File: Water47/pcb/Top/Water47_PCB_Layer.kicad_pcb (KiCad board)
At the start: 2 copper layers, 260 x 76.5 mm, 51 parts, among them SW1 Esc, SW10 O, SW11 P, SW12 -, SW13 Del, SW14 Cmd, SW15 A, SW16 S, SW17 D, SW18 F, SW19 G, SW2 Q, SW20 H, SW21 J, SW22 K, SW23 L, SW24 ;, SW25 Bs, SW26 Shift(L), SW27 Z, SW28 X, SW29 C, SW3 W, SW30 V, SW31 B, SW32 N, SW33 M, SW34 ,, SW35 ., SW36 Shift(R), SW37 Fn, SW38 Ctrl(L), SW39 Win(L), SW4 E, SW40 Alt(L), SW41 Shift(C), SW42 Fn(C), SW43 Enter, SW44 ←, SW45 ↓, SW46 ↑, SW47 →, SW5 R, SW6 T, SW7 Y, SW8 U, SW9 I

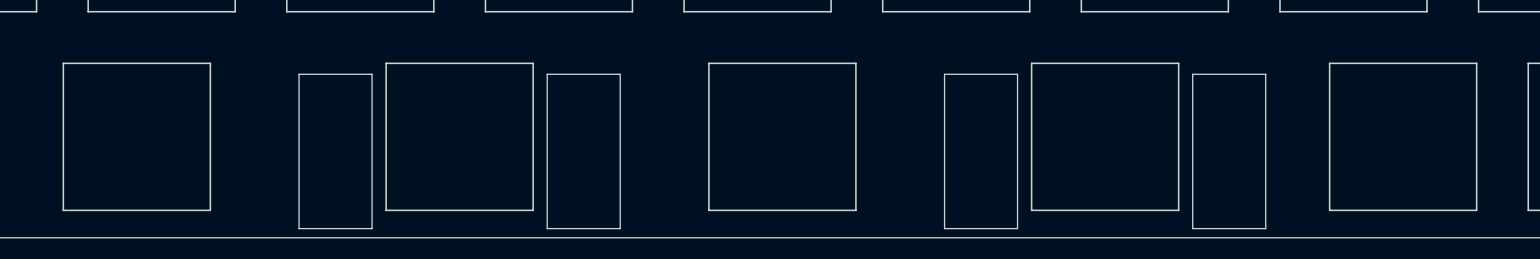
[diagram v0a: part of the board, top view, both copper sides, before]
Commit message: feat: change key layout
2u -> 1.75u to not put stabilizer
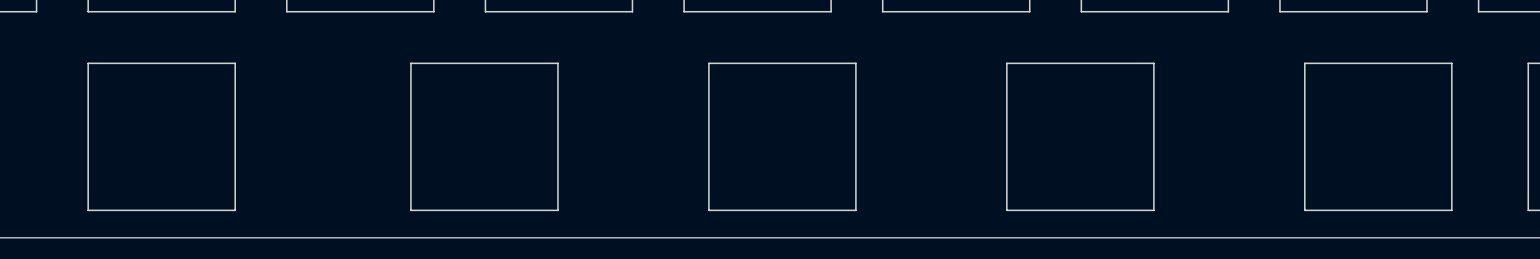
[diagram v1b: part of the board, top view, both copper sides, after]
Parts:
- SW40: footprint kbd_SW_Hole:SW_Hole_1.25u -> kbd_SW_Hole:SW_Hole_1.5u
- SW41, SW43: footprint kbd_SW_Hole:SW_Hole_2u -> kbd_SW_Hole:SW_Hole_1.75u
- SW44: footprint kbd_SW_Hole:SW_Hole_1u -> kbd_SW_Hole:SW_Hole_1.25u
- moved SW40 2.38 mm to (150.0, 150.0)
- moved SW44 2.38 mm to (266.7, 150.0)
- moved SW41 2.38 mm to (181.0, 150.0)
- moved SW43 2.38 mm to (238.1, 150.0)
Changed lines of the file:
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@@
   )
   (net 0 "")
-  (footprint "kbd_SW_Hole:SW_Hole_2u" (layer "F.Cu")
-    (at 178.59375 150.01875)
-    (property "Sheetfile" "Water47_PCB_Layer.kicad_sch")
-    (property "Sheetname" "")
-    (attr through_hole)
-    (fp_text reference "SW41" (at 7 8.1) (layer "Edge.Cuts") hide
+  (footprint "kbd_SW_Hole:SW_Hole_1.75u" (layer "F.Cu")
+    (at 180.975 150.01875)
+    (property "Sheetfile" "Water47_PCB_Layer.kicad_sch")
+    (property "Sheetname" "")
+    (attr through_hole)
+    (fp_text reference "SW41" (at 7 8.1) (layer "F.SilkS") hide
       (effects (font (size 1 1) (thickness 0.15)))
     )
@@
       (effects (font (size 1 1) (thickness 0.15)))
     )
-    (fp_line (start -8.4 -6) (end -8.4 8.8) (layer "Edge.Cuts") (width 0.12))
-    (fp_line (start -15.4 8.8) (end -15.4 -6) (layer "Edge.Cuts") (width 0.12))
-    (fp_line (start -8.4 8.8) (end -15.4 8.8) (layer "Edge.Cuts") (width 0.12))
-    (fp_line (start 15.4 -6) (end 8.4 -6) (layer "Edge.Cuts") (width 0.12))
-    (fp_line (start 7.05 7.05) (end -7.05 7.05) (layer "Edge.Cuts") (width 0.15))
-    (fp_line (start 7.05 -7.05) (end 7.05 7.05) (layer "Edge.Cuts") (width 0.15))
-    (fp_line (start 8.4 8.8) (end 15.4 8.8) (layer "Edge.Cuts") (width 0.12))
-    (fp_line (start -7.05 -7.05) (end 7.05 -7.05) (layer "Edge.Cuts") (width 0.15))
-    (fp_line (start 15.4 8.8) (end 15.4 -6) (layer "Edge.Cuts") (width 0.12))
-    (fp_line (start -15.4 -6) (end -8.4 -6) (layer "Edge.Cuts") (width 0.12))
-    (fp_line (start 8.4 -6) (end 8.4 8.8) (layer "Edge.Cuts") (width 0.12))
-    (fp_line (start -7.05 7.05) (end -7.05 -7.05) (layer "Edge.Cuts") (width 0.15))
-    (fp_line (start -19.05 9.525) (end 19.05 9.525) (layer "F.Fab") (width 0.15))
-    (fp_line (start 19.05 9.525) (end 19.05 -9.525) (layer "F.Fab") (width 0.15))
-    (fp_line (start -19.05 -9.525) (end -19.05 9.525) (layer "F.Fab") (width 0.15))
-    (fp_line (start 19.05 -9.525) (end -19.05 -9.525) (layer "F.Fab") (width 0.15))
+    (fp_line (start -7.05 7.05) (end -7.05 -7.05) (layer "Edge.Cuts") (width 0.15))
+    (fp_line (start 7.05 7.05) (end -7.05 7.05) (layer "Edge.Cuts") (width 0.15))
+    (fp_line (start -7.05 -7.05) (end 7.05 -7.05) (layer "Edge.Cuts") (width 0.15))
+    (fp_line (start 7.05 -7.05) (end 7.05 7.05) (layer "Edge.Cuts") (width 0.15))
+    (fp_line (start -16.66875 9.525) (end 16.66875 9.525) (layer "F.Fab") (width 0.15))
+    (fp_line (start -16.66875 -9.525) (end -16.66875 9.525) (layer "F.Fab") (width 0.15))
+    (fp_line (start 16.66875 -9.525) (end -16.66875 -9.525) (layer "F.Fab") (width 0.15))
+    (fp_line (start 16.66875 9.525) (end 16.66875 -9.525) (layer "F.Fab") (width 0.15))
   )
   (footprint "kbd_SW_Hole:SW_Hole_1u" (layer "F.Cu")
@@
     (fp_line (start 9.525 -9.525) (end -9.525 -9.525) (layer "F.Fab") (width 0.15))
   )
-  (footprint "kbd_SW_Hole:SW_Hole_1u" (layer "F.Cu")
-    (at 269.08125 150.01875)
+  (footprint "kbd_SW_Hole:SW_Hole_1.25u" (layer "F.Cu")
+    (at 266.7 150.01875)
     (property "Sheetfile" "Water47_PCB_Layer.kicad_sch")
     (property "Sheetname" "")
@@
       (effects (font (size 1 1) (thickness 0.15)))
     )
-    (fp_line (start 7.05 -7.05) (end 7.05 7.05) (layer "Edge.Cuts") (width 0.15))
-    (fp_line (start -7.05 7.05) (end -7.05 -7.05) (layer "Edge.Cuts") (width 0.15))
-    (fp_line (start 7.05 7.05) (end -7.05 7.05) (layer "Edge.Cuts") (width 0.15))
-    (fp_line (start -7.05 -7.05) (end 7.05 -7.05) (layer "Edge.Cuts") (width 0.15))
-    (fp_line (start -9.525 9.525) (end 9.525 9.525) (layer "F.Fab") (width 0.15))
-    (fp_line (start -9.525 -9.525) (end -9.525 9.525) (layer "F.Fab") (width 0.15))
-    (fp_line (start 9.525 -9.525) (end -9.525 -9.525) (layer "F.Fab") (width 0.15))
-    (fp_line (start 9.525 9.525) (end 9.525 -9.525) (layer "F.Fab") (width 0.15))
+    (fp_line (start -7.05 -7.05) (end 7.05 -7.05) (layer "Edge.Cuts") (width 0.15))
+    (fp_line (start 7.05 -7.05) (end 7.05 7.05) (layer "Edge.Cuts") (width 0.15))
+    (fp_line (start 7.05 7.05) (end -7.05 7.05) (layer "Edge.Cuts") (width 0.15))
+    (fp_line (start -7.05 7.05) (end -7.05 -7.05) (layer "Edge.Cuts") (width 0.15))
+    (fp_line (start -11.90625 -9.525) (end -11.90625 9.525) (layer "F.Fab") (width 0.15))
+    (fp_line (start 11.90625 -9.525) (end -11.90625 -9.525) (layer "F.Fab") (width 0.15))
+    (fp_line (start 11.90625 9.525) (end 11.90625 -9.525) (layer "F.Fab") (width 0.15))
+    (fp_line (start -11.90625 9.525) (end 11.90625 9.525) (layer "F.Fab") (width 0.15))
   )
   (footprint "kbd_SW_Hole:SW_Hole_1u" (layer "F.Cu")
@@
     (fp_line (start -16.66875 -9.525) (end -16.66875 9.525) (layer "F.Fab") (width 0.15))
   )
-  (footprint "kbd_SW_Hole:SW_Hole_1.25u" (layer "F.Cu")
-    (at 147.6375 150.01875)
+  (footprint "kbd_SW_Hole:SW_Hole_1.5u" (layer "F.Cu")
+    (at 150.01875 150.01875)
     (property "Sheetfile" "Water47_PCB_Layer.kicad_sch")
     (property "Sheetname" "")
@@
     (fp_line (start -7.05 7.05) (end -7.05 -7.05) (layer "Edge.Cuts") (width 0.15))
     (fp_line (start 7.05 7.05) (end -7.05 7.05) (layer "Edge.Cuts") (width 0.15))
-    (fp_line (start 11.90625 -9.525) (end -11.90625 -9.525) (layer "F.Fab") (width 0.15))
-    (fp_line (start -11.90625 9.525) (end 11.90625 9.525) (layer "F.Fab") (width 0.15))
-    (fp_line (start -11.90625 -9.525) (end -11.90625 9.525) (layer "F.Fab") (width 0.15))
-    (fp_line (start 11.90625 9.525) (end 11.90625 -9.525) (layer "F.Fab") (width 0.15))
+    (fp_line (start -14.2875 -9.525) (end -14.2875 9.525) (layer "F.Fab") (width 0.15))
+    (fp_line (start 14.2875 -9.525) (end -14.2875 -9.525) (layer "F.Fab") (width 0.15))
+    (fp_line (start 14.2875 9.525) (end 14.2875 -9.525) (layer "F.Fab") (width 0.15))
+    (fp_line (start -14.2875 9.525) (end 14.2875 9.525) (layer "F.Fab") (width 0.15))
   )
   (footprint "kbd_SW_Hole:SW_Hole_1u" (layer "F.Cu")
@@
     (fp_line (start 9.525 -9.525) (end -9.525 -9.525) (layer "F.Fab") (width 0.15))
   )
-  (footprint "kbd_SW_Hole:SW_Hole_2u" (layer "F.Cu")
-    (at 240.5 150.01875)
-    (property "Sheetfile" "Water47_PCB_Layer.kicad_sch")
-    (property "Sheetname" "")
-    (attr through_hole)
-    (fp_text reference "SW43" (at 7 8.1) (layer "Edge.Cuts") hide
+  (footprint "kbd_SW_Hole:SW_Hole_1.75u" (layer "F.Cu")
+    (at 238.125 150.01875)
+    (property "Sheetfile" "Water47_PCB_Layer.kicad_sch")
+    (property "Sheetname" "")
+    (attr through_hole)
+    (fp_text reference "SW43" (at 7 8.1) (layer "F.SilkS") hide
       (effects (font (size 1 1) (thickness 0.15)))
     )
@@
       (effects (font (size 1 1) (thickness 0.15)))
     )
-    (fp_line (start -7.05 7.05) (end -7.05 -7.05) (layer "Edge.Cuts") (width 0.15))
-    (fp_line (start -8.4 8.8) (end -15.4 8.8) (layer "Edge.Cuts") (width 0.12))
-    (fp_line (start 7.05 7.05) (end -7.05 7.05) (layer "Edge.Cuts") (width 0.15))
-    (fp_line (start 15.4 -6) (end 8.4 -6) (layer "Edge.Cuts") (width 0.12))
-    (fp_line (start -15.4 8.8) (end -15.4 -6) (layer "Edge.Cuts") (width 0.12))
-    (fp_line (start 8.4 8.8) (end 15.4 8.8) (layer "Edge.Cuts") (width 0.12))
-    (fp_line (start -15.4 -6) (end -8.4 -6) (layer "Edge.Cuts") (width 0.12))
-    (fp_line (start 7.05 -7.05) (end 7.05 7.05) (layer "Edge.Cuts") (width 0.15))
-    (fp_line (start 8.4 -6) (end 8.4 8.8) (layer "Edge.Cuts") (width 0.12))
-    (fp_line (start 15.4 8.8) (end 15.4 -6) (layer "Edge.Cuts") (width 0.12))
-    (fp_line (start -8.4 -6) (end -8.4 8.8) (layer "Edge.Cuts") (width 0.12))
-    (fp_line (start -7.05 -7.05) (end 7.05 -7.05) (layer "Edge.Cuts") (width 0.15))
-    (fp_line (start 19.05 9.525) (end 19.05 -9.525) (layer "F.Fab") (width 0.15))
-    (fp_line (start -19.05 -9.525) (end -19.05 9.525) (layer "F.Fab") (width 0.15))
-    (fp_line (start 19.05 -9.525) (end -19.05 -9.525) (layer "F.Fab") (width 0.15))
-    (fp_line (start -19.05 9.525) (end 19.05 9.525) (layer "F.Fab") (width 0.15))
+    (fp_line (start -7.05 -7.05) (end 7.05 -7.05) (layer "Edge.Cuts") (width 0.15))
+    (fp_line (start -7.05 7.05) (end -7.05 -7.05) (layer "Edge.Cuts") (width 0.15))
+    (fp_line (start 7.05 7.05) (end -7.05 7.05) (layer "Edge.Cuts") (width 0.15))
+    (fp_line (start 7.05 -7.05) (end 7.05 7.05) (layer "Edge.Cuts") (width 0.15))
+    (fp_line (start -16.66875 9.525) (end 16.66875 9.525) (layer "F.Fab") (width 0.15))
+    (fp_line (start 16.66875 9.525) (end 16.66875 -9.525) (layer "F.Fab") (width 0.15))
+    (fp_line (start -16.66875 -9.525) (end -16.66875 9.525) (layer "F.Fab") (width 0.15))
+    (fp_line (start 16.66875 -9.525) (end -16.66875 -9.525) (layer "F.Fab") (width 0.15))
   )
   (footprint "kbd_SW_Hole:SW_Hole_1.25u" (layer "F.Cu")
